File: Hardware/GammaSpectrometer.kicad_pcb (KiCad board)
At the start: 2 copper layers, 100 x 100 mm, 449 parts, among them U10 LT3093, U11 AP2112K-3.3, U12 AP2112K-1.2, U13 REF3220AMDBVREP, U14 LT3042, U15 LT3042, U16 LT8330IS6, U17 NCP163ASN330T1G (3v3), U18 5PB1102PGGK, U19 MX25L1606EM1I-12G, U2 REF3220AMDBVREP, U3 LTC6268IS6, U4 AD8139, U5 TPS7A4901, U6 ICE40HX4K-TQ144, U7 AP2112K-3.3, U7 LT8330IS6, U7 XLH736065.000000I, U8 AP2112K-1.2, U8 LT8330IS6, U9 LT3093

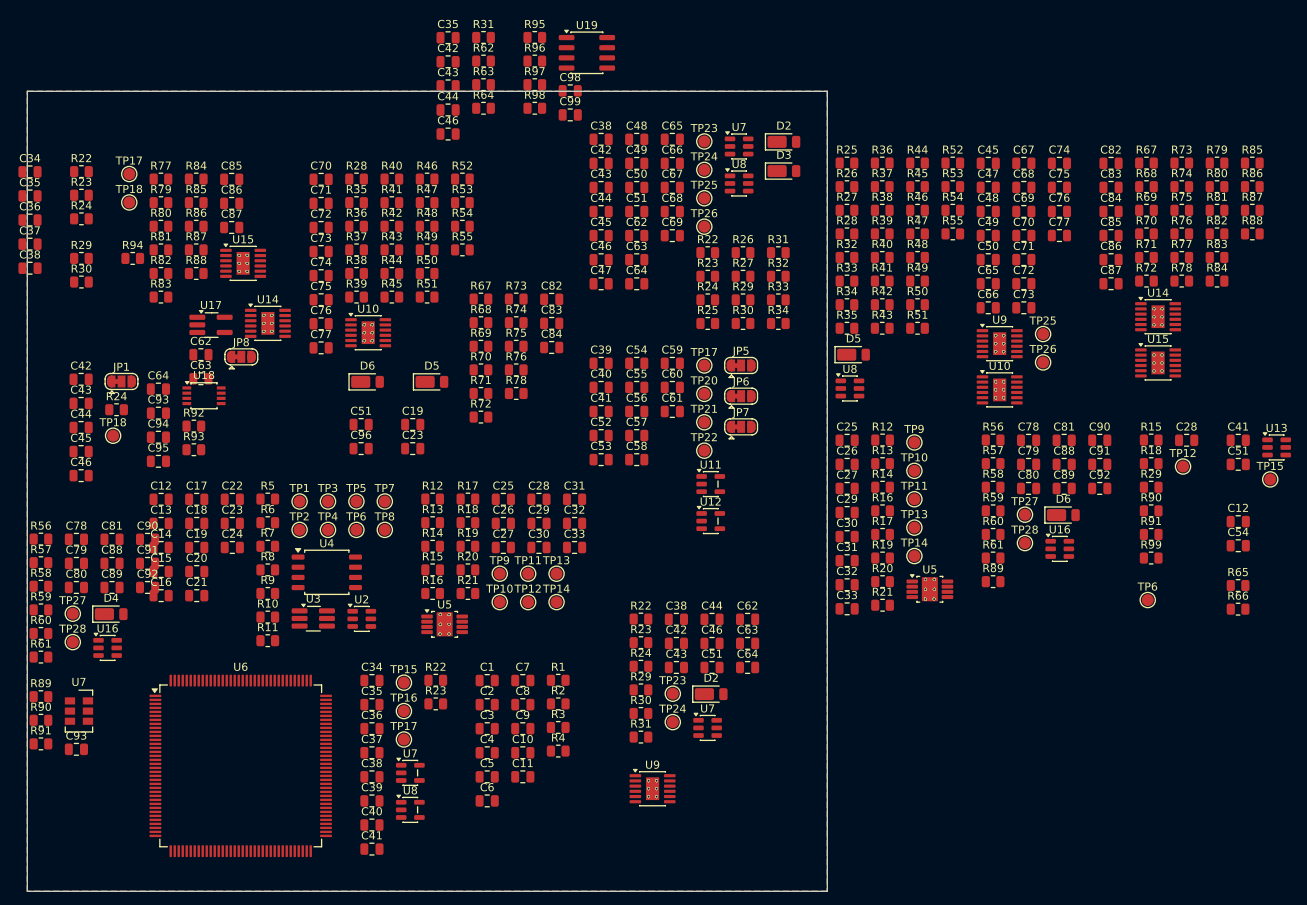
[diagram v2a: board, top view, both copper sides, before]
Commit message: fix: #134
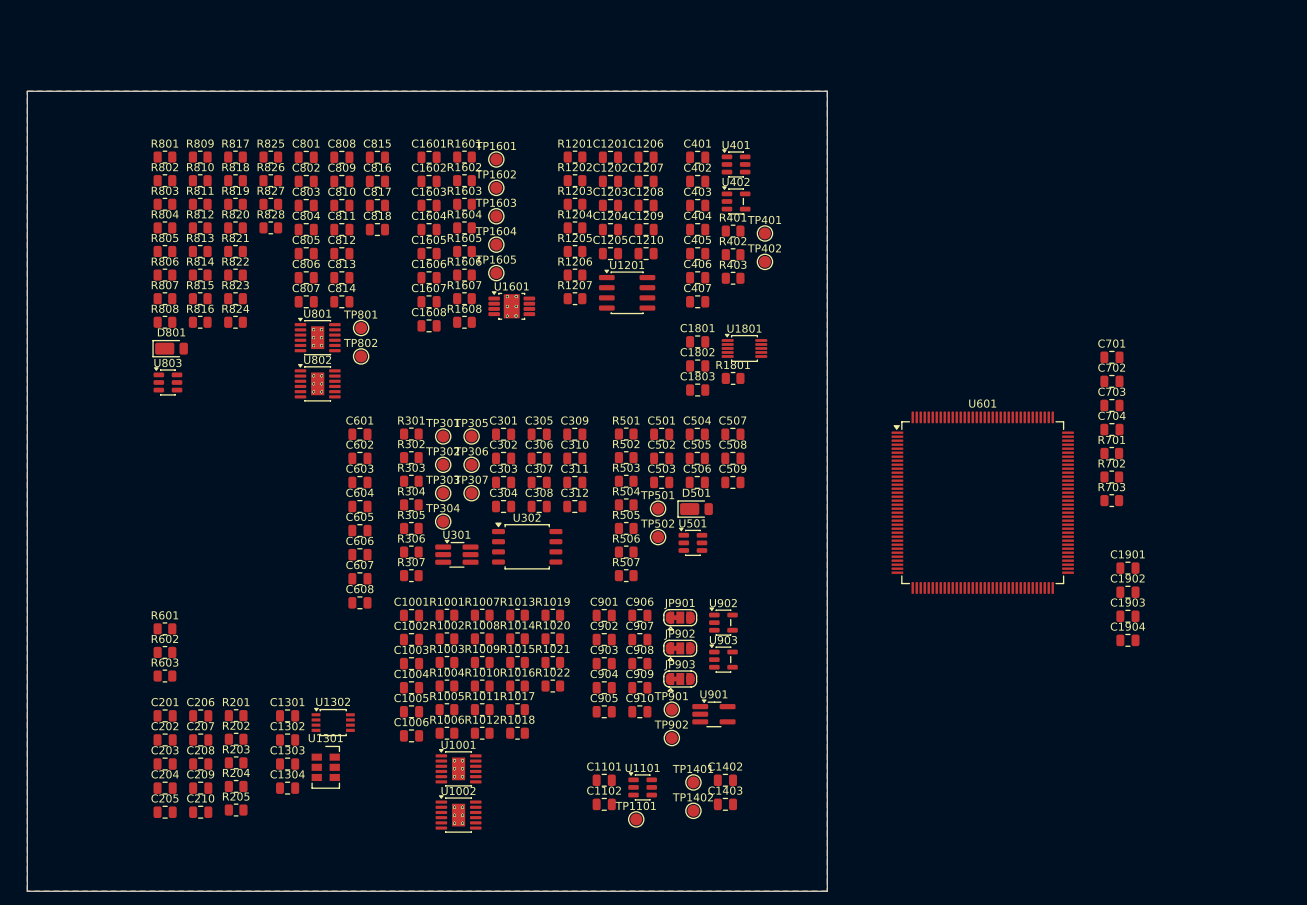
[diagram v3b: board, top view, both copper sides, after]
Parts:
- removed C1, C10, C12, C13, C14, C18, C19 (x2), C2, C28 (x2), C34, C35 (x2), C36 (x2), C37 (x2), C38, C39, C4, C41, C42, C43, C44, C46 (x3), C5, C50 (x2), C51, C52, C53, C54, C58, C59, C64 (x3), C67 (x2), C7, C80 (x2), C9, C92 (x2), C94, C96, C98: 100n, Capacitor_SMD:C_0805_2012Metric
- removed C11, C15, C16, C22, C23 (x2), C29 (x2), C30 (x2), C31 (x2), C51, C93, C95, C99: 10n, Capacitor_SMD:C_0805_2012Metric
- removed C12, C41: 470n, Capacitor_SMD:C_0805_2012Metric
- removed C17: 33p, Capacitor_SMD:C_0805_2012Metric
- removed C20, C21: 1p, Capacitor_SMD:C_0805_2012Metric
- removed C24: 22p, Capacitor_SMD:C_0805_2012Metric
- removed C25 (x2), C32 (x2): 10u/60V, Capacitor_SMD:C_0805_2012Metric
- removed C26 (x2), C33 (x2): 100n/60V, Capacitor_SMD:C_0805_2012Metric
- removed C27 (x2): TBD, Capacitor_SMD:C_0805_2012Metric
- removed C3, C38 (x2), C41, C42 (x3), C44 (x3), C46, C47 (x2), C48 (x2), C49 (x2), C51 (x2), C55, C6, C61, C62 (x2), C65 (x2), C66 (x2), C78 (x2), C79 (x2), C8, C89 (x2), C90 (x2), C91 (x2): 10u, Capacitor_SMD:C_0805_2012Metric
- removed C34, C35, C38, C39, C40 (x2), C43, C45, C54, C56, C57, C60, C62, C63 (x3), C68 (x2), C69 (x2), C81 (x2): 1u, Capacitor_SMD:C_0805_2012Metric
- removed C43 (x2), C45 (x2), C88 (x2): 10p, Capacitor_SMD:C_0805_2012Metric
- removed C70 (x2), C73 (x2), C76 (x2), C77 (x2): 4u7, Capacitor_SMD:C_0805_2012Metric
- removed C71 (x2), C75 (x2), C83 (x2), C86 (x2): 4u7 X7R, Capacitor_SMD:C_0805_2012Metric
- removed C72 (x2), C74 (x2), C82 (x2), C84 (x2), C85 (x2), C87 (x2), C93: 10u/16v, Capacitor_SMD:C_0805_2012Metric
- removed D2 (x2), D3, D4: DFLS140L-7, Diode_SMD:D_PowerDI-123
- removed D5 (x2), D6 (x2): DFLS1100-7, Diode_SMD:D_PowerDI-123
- removed JP1, JP5: DVCC_ADC_ON, Jumper:SolderJumper-3_P1.3mm_Bridged12_RoundedPad1.0x1.5mm
- removed JP6: 3V3_ON, Jumper:SolderJumper-3_P1.3mm_Bridged12_RoundedPad1.0x1.5mm
- removed JP7: 1V2_ON, Jumper:SolderJumper-3_P1.3mm_Bridged12_RoundedPad1.0x1.5mm
- removed JP8: DVCC_CLK_ON, Jumper:SolderJumper-3_P1.3mm_Bridged12_RoundedPad1.0x1.5mm
- removed R1, R13, R14 (x2), R18 (x2), R2, R22, R23, R24, R28 (x2), R29 (x2), R3, R30, R31 (x2), R34 (x2), R35 (x2), R38 (x2), R4, R40 (x2), R43 (x2), R45 (x2), R47 (x2), R48 (x2), R53 (x2), R54 (x2), R58, R65, R66, R68 (x2), R69 (x2), R70 (x2), R75 (x2), R76 (x2), R79 (x2), R80 (x2), R81 (x2), R86 (x2), R87 (x2), R89, R90 (x2), R91, R99: TBD, Resistor_SMD:R_0805_2012Metric
- removed R10, R11: 50R, Resistor_SMD:R_0805_2012Metric
- removed R12 (x2), R13, R15 (x2), R22, R23, R24 (x3), R27 (x2), R29 (x2), R30 (x2), R32 (x2), R33 (x2), R39 (x2), R41 (x2), R42 (x2), R44 (x2), R46 (x2), R49 (x2), R51 (x2), R55 (x2), R56 (x2), R57 (x2), R61 (x2), R67 (x2), R72 (x2), R74 (x2), R77 (x2), R78 (x2), R83 (x2), R85 (x2), R88 (x2), R89, R91, R92, R93, R94, R96, R97: 0R, Resistor_SMD:R_0805_2012Metric
- removed R16 (x2), R21 (x2), R23 (x2), R26 (x2), R31, R5, R60 (x2), R63, R95: 10k, Resistor_SMD:R_0805_2012Metric
- removed R17 (x2): 2M, Resistor_SMD:R_0805_2012Metric
- removed R19 (x2): 220k, Resistor_SMD:R_0805_2012Metric
- removed R20 (x2): 33k, Resistor_SMD:R_0805_2012Metric
- removed R22 (x2), R59 (x2): 200k, Resistor_SMD:R_0805_2012Metric
- removed R25 (x2): 68k1, Resistor_SMD:R_0805_2012Metric
- removed R36 (x2), R52 (x2): 19k5, Resistor_SMD:R_0805_2012Metric
- removed R37 (x2): 27k9, Resistor_SMD:R_0805_2012Metric
- removed R50 (x2), R71 (x2): 49k9, Resistor_SMD:R_0805_2012Metric
- removed R58: 47k, Resistor_SMD:R_0805_2012Metric
- removed R6, R7: 499R, Resistor_SMD:R_0805_2012Metric
- removed R62: 100R, Resistor_SMD:R_0805_2012Metric
- removed R64: 680R, Resistor_SMD:R_0805_2012Metric
- removed R73 (x2), R84 (x2): 1k24, Resistor_SMD:R_0805_2012Metric
- removed R8, R9: 1k, Resistor_SMD:R_0805_2012Metric
- removed R82 (x2): 24k9, Resistor_SMD:R_0805_2012Metric
- removed R98: 22R, Resistor_SMD:R_0805_2012Metric
- removed TP1, TP10 (x2), TP11 (x2), TP12 (x2), TP13 (x2), TP14 (x2), TP15, TP16, TP17 (x2), TP18, TP2, TP20, TP21, TP22, TP23 (x2), TP24 (x2), TP25 (x2), TP26 (x2), TP27 (x2), TP28 (x2), TP3, TP4, TP5, TP6 (x2), TP7, TP8, TP9 (x2): TestPoint, TestPoint:TestPoint_Pad_D1.5mm
- removed TP15: REF_OUT, TestPoint:TestPoint_Pad_D1.5mm
- removed TP17: GND, TestPoint:TestPoint_Pad_D1.5mm
- removed TP18: +V_IN, TestPoint:TestPoint_Pad_D1.5mm
- removed U10 (x2), U9 (x2): LT3093, Package_SO:MSOP-12-1EP_3x4.039mm_P0.65mm_EP1.651x2.845mm_ThermalVias
- removed U11, U7: AP2112K-3.3, Package_TO_SOT_SMD:SOT-23-5
- removed U12, U8: AP2112K-1.2, Package_TO_SOT_SMD:SOT-23-5
- removed U13, U2: REF3220AMDBVREP, Package_TO_SOT_SMD:SOT-23-6
- removed U14 (x2), U15 (x2): LT3042, Package_SO:MSOP-12-1EP_3x4.039mm_P0.65mm_EP1.651x2.845mm_ThermalVias
- removed U16 (x2), U7 (x2), U8 (x2): LT8330IS6, Package_TO_SOT_SMD:TSOT-23-6
- removed U17: NCP163ASN330T1G (3v3), Package_TO_SOT_SMD:TSOT-23-5_HandSoldering
- removed U18: 5PB1102PGGK, Package_SO:TSSOP-8_3x3mm_P0.65mm
- removed U19: MX25L1606EM1I-12G, Package_SO:SOP-8_3.76x4.96mm_P1.27mm
- removed U3: LTC6268IS6, Package_TO_SOT_SMD:TSOT-23-6_HandSoldering
- removed U4: AD8139, Package_SO:SOIC-8_5.3x5.3mm_P1.27mm
- removed U5 (x2): TPS7A4901, Package_SO:Texas_DGN0008B_VSSOP-8-1EP_3x3mm_P0.65mm_EP2x3mm_Mask1.88x1.98mm_ThermalVias
- removed U6: ICE40HX4K-TQ144, Package_QFP:TQFP-144_20x20mm_P0.5mm
- removed U7: XLH736065.000000I, Oscillator:Oscillator_SMD_IDT_JS6-6_5.0x3.2mm_P1.27mm
- added C1001: 10u/16v, Capacitor_SMD:C_0805_2012Metric, F.Cu at (143.0, 90.5)
- added C1002: 10u/16v, Capacitor_SMD:C_0805_2012Metric, F.Cu at (143.0, 93.5)
- added C1003: 4u7 X7R, Capacitor_SMD:C_0805_2012Metric, F.Cu at (143.0, 96.5)
- added C1004: 4u7 X7R, Capacitor_SMD:C_0805_2012Metric, F.Cu at (143.0, 99.6)
- added C1005: 10u/16v, Capacitor_SMD:C_0805_2012Metric, F.Cu at (143.0, 102.6)
- added C1006: 10u/16v, Capacitor_SMD:C_0805_2012Metric, F.Cu at (143.0, 105.6)
- added C1101: 470n, Capacitor_SMD:C_0805_2012Metric, F.Cu at (167.1, 111.1)
- added C1102: 10n, Capacitor_SMD:C_0805_2012Metric, F.Cu at (167.1, 114.1)
- added C1201: 10u, Capacitor_SMD:C_0805_2012Metric, F.Cu at (167.9, 33.3)
- added C1202: 10u, Capacitor_SMD:C_0805_2012Metric, F.Cu at (167.9, 36.3)
- added C1203: 10u, Capacitor_SMD:C_0805_2012Metric, F.Cu at (167.9, 39.3)
- added C1204: 100n, Capacitor_SMD:C_0805_2012Metric, F.Cu at (167.9, 42.3)
- added C1205: 100n, Capacitor_SMD:C_0805_2012Metric, F.Cu at (167.9, 45.3)
- added C1206: 100n, Capacitor_SMD:C_0805_2012Metric, F.Cu at (172.3, 33.3)
- added C1207: 100n, Capacitor_SMD:C_0805_2012Metric, F.Cu at (172.3, 36.3)
- added C1208: 100n, Capacitor_SMD:C_0805_2012Metric, F.Cu at (172.3, 39.3)
- added C1209: 100n, Capacitor_SMD:C_0805_2012Metric, F.Cu at (172.3, 42.3)
- added C1210: 10n, Capacitor_SMD:C_0805_2012Metric, F.Cu at (172.3, 45.3)
- added C1301: 100n, Capacitor_SMD:C_0805_2012Metric, F.Cu at (127.5, 103.1)
- added C1302: 10n, Capacitor_SMD:C_0805_2012Metric, F.Cu at (127.5, 106.1)
- added C1303: 100n, Capacitor_SMD:C_0805_2012Metric, F.Cu at (127.5, 109.1)
- added C1304: 10n, Capacitor_SMD:C_0805_2012Metric, F.Cu at (127.5, 112.1)
- added C1402: 100n, Capacitor_SMD:C_0805_2012Metric, F.Cu at (182.3, 111.1)
- added C1403: 100n, Capacitor_SMD:C_0805_2012Metric, F.Cu at (182.3, 114.1)
- added C1601: 10u/60V, Capacitor_SMD:C_0805_2012Metric, F.Cu at (145.2, 33.3)
- added C1602: 100n/60V, Capacitor_SMD:C_0805_2012Metric, F.Cu at (145.2, 36.3)
- added C1603: TBD, Capacitor_SMD:C_0805_2012Metric, F.Cu at (145.2, 39.3)
- added C1604: 10n, Capacitor_SMD:C_0805_2012Metric, F.Cu at (145.2, 42.3)
- added C1605: 10n, Capacitor_SMD:C_0805_2012Metric, F.Cu at (145.2, 45.3)
- added C1606: 10n, Capacitor_SMD:C_0805_2012Metric, F.Cu at (145.2, 48.3)
- added C1607: 10u/60V, Capacitor_SMD:C_0805_2012Metric, F.Cu at (145.2, 51.3)
- added C1608: 100n/60V, Capacitor_SMD:C_0805_2012Metric, F.Cu at (145.2, 54.3)
- added C1801: 10u, Capacitor_SMD:C_0805_2012Metric, F.Cu at (178.8, 56.3)
- added C1802: 100n, Capacitor_SMD:C_0805_2012Metric, F.Cu at (178.8, 59.3)
- added C1803: 100n, Capacitor_SMD:C_0805_2012Metric, F.Cu at (178.8, 62.3)
- added C1901: 10u, Capacitor_SMD:C_0805_2012Metric, F.Cu at (232.6, 84.6)
- added C1902: 100n, Capacitor_SMD:C_0805_2012Metric, F.Cu at (232.6, 87.6)
- added C1903: 10u, Capacitor_SMD:C_0805_2012Metric, F.Cu at (232.6, 90.6)
- added C1904: 100n, Capacitor_SMD:C_0805_2012Metric, F.Cu at (232.6, 93.6)
- added C201: 100n, Capacitor_SMD:C_0805_2012Metric, F.Cu at (112.2, 103.1)
- added C202: 10u, Capacitor_SMD:C_0805_2012Metric, F.Cu at (112.2, 106.1)
- added C203: 100n, Capacitor_SMD:C_0805_2012Metric, F.Cu at (112.2, 109.1)
- added C204: 100n, Capacitor_SMD:C_0805_2012Metric, F.Cu at (112.2, 112.1)
- added C205: 100n, Capacitor_SMD:C_0805_2012Metric, F.Cu at (112.2, 115.1)
- added C206: 10u, Capacitor_SMD:C_0805_2012Metric, F.Cu at (116.7, 103.1)
- added C207: 10u, Capacitor_SMD:C_0805_2012Metric, F.Cu at (116.7, 106.1)
- added C208: 100n, Capacitor_SMD:C_0805_2012Metric, F.Cu at (116.7, 109.1)
- added C209: 100n, Capacitor_SMD:C_0805_2012Metric, F.Cu at (116.7, 112.1)
- added C210: 10n, Capacitor_SMD:C_0805_2012Metric, F.Cu at (116.7, 115.1)
- added C301: 100n, Capacitor_SMD:C_0805_2012Metric, F.Cu at (154.5, 67.9)
- added C302: 100n, Capacitor_SMD:C_0805_2012Metric, F.Cu at (154.5, 70.9)
- added C303: 10n, Capacitor_SMD:C_0805_2012Metric, F.Cu at (154.5, 73.9)
- added C304: 10n, Capacitor_SMD:C_0805_2012Metric, F.Cu at (154.5, 76.9)
- added C305: 33p, Capacitor_SMD:C_0805_2012Metric, F.Cu at (159.0, 67.9)
- added C306: 100n, Capacitor_SMD:C_0805_2012Metric, F.Cu at (159.0, 70.9)
- added C307: 100n, Capacitor_SMD:C_0805_2012Metric, F.Cu at (159.0, 73.9)
- added C308: 1p, Capacitor_SMD:C_0805_2012Metric, F.Cu at (159.0, 76.9)
- added C309: 1p, Capacitor_SMD:C_0805_2012Metric, F.Cu at (163.4, 67.9)
- added C310: 10n, Capacitor_SMD:C_0805_2012Metric, F.Cu at (163.4, 70.9)
- added C311: 10n, Capacitor_SMD:C_0805_2012Metric, F.Cu at (163.4, 73.9)
- added C312: 22p, Capacitor_SMD:C_0805_2012Metric, F.Cu at (163.4, 76.9)
- added C401: 10u, Capacitor_SMD:C_0805_2012Metric, F.Cu at (178.8, 33.3)
- added C402: 10u, Capacitor_SMD:C_0805_2012Metric, F.Cu at (178.8, 36.3)
- added C403: TBD, Capacitor_SMD:C_0805_2012Metric, F.Cu at (178.8, 39.3)
- added C404: 100n, Capacitor_SMD:C_0805_2012Metric, F.Cu at (178.8, 42.3)
- added C405: 100n, Capacitor_SMD:C_0805_2012Metric, F.Cu at (178.8, 45.3)
- added C406: 10n, Capacitor_SMD:C_0805_2012Metric, F.Cu at (178.8, 48.3)
- added C407: 10n, Capacitor_SMD:C_0805_2012Metric, F.Cu at (178.8, 51.3)
- added C501: 10u, Capacitor_SMD:C_0805_2012Metric, F.Cu at (174.3, 67.9)
- added C502: 10u, Capacitor_SMD:C_0805_2012Metric, F.Cu at (174.3, 70.9)
- added C503: 100n, Capacitor_SMD:C_0805_2012Metric, F.Cu at (174.3, 73.9)
- added C504: 1u, Capacitor_SMD:C_0805_2012Metric, F.Cu at (178.7, 67.9)
- added C505: 10p, Capacitor_SMD:C_0805_2012Metric, F.Cu at (178.7, 70.9)
- added C506: 10u, Capacitor_SMD:C_0805_2012Metric, F.Cu at (178.7, 73.9)
- added C507: 10u, Capacitor_SMD:C_0805_2012Metric, F.Cu at (183.2, 67.9)
- added C508: 10u, Capacitor_SMD:C_0805_2012Metric, F.Cu at (183.2, 70.9)
- added C509: 100n, Capacitor_SMD:C_0805_2012Metric, F.Cu at (183.2, 73.9)
- added C601: 100n, Capacitor_SMD:C_0805_2012Metric, F.Cu at (136.6, 67.9)
- added C602: 100n, Capacitor_SMD:C_0805_2012Metric, F.Cu at (136.6, 70.9)
- added C603: 100n, Capacitor_SMD:C_0805_2012Metric, F.Cu at (136.6, 73.9)
- added C604: 100n, Capacitor_SMD:C_0805_2012Metric, F.Cu at (136.6, 76.9)
- added C605: 10u, Capacitor_SMD:C_0805_2012Metric, F.Cu at (136.6, 79.9)
- added C606: 10u, Capacitor_SMD:C_0805_2012Metric, F.Cu at (136.6, 82.9)
- added C607: 10u, Capacitor_SMD:C_0805_2012Metric, F.Cu at (136.6, 85.9)
- added C608: 10u, Capacitor_SMD:C_0805_2012Metric, F.Cu at (136.6, 88.9)
- added C701: 10u, Capacitor_SMD:C_0805_2012Metric, F.Cu at (230.6, 58.3)
- added C702: 100n, Capacitor_SMD:C_0805_2012Metric, F.Cu at (230.6, 61.3)
- added C703: 10u, Capacitor_SMD:C_0805_2012Metric, F.Cu at (230.6, 64.3)
- added C704: 100n, Capacitor_SMD:C_0805_2012Metric, F.Cu at (230.6, 67.3)
- added C801: 10u, Capacitor_SMD:C_0805_2012Metric, F.Cu at (129.9, 33.3)
- added C802: 10u/16v, Capacitor_SMD:C_0805_2012Metric, F.Cu at (129.9, 36.3)
- added C803: 10u/16v, Capacitor_SMD:C_0805_2012Metric, F.Cu at (129.9, 39.3)
- added C804: 10u, Capacitor_SMD:C_0805_2012Metric, F.Cu at (129.9, 42.3)
- added C805: 100n, Capacitor_SMD:C_0805_2012Metric, F.Cu at (129.9, 45.3)
- added C806: 4u7 X7R, Capacitor_SMD:C_0805_2012Metric, F.Cu at (129.9, 48.3)
- added C807: 4u7 X7R, Capacitor_SMD:C_0805_2012Metric, F.Cu at (129.9, 51.3)
- added C808: 1u, Capacitor_SMD:C_0805_2012Metric, F.Cu at (134.3, 33.3)
- added C809: 1u, Capacitor_SMD:C_0805_2012Metric, F.Cu at (134.3, 36.3)
- added C810: 4u7, Capacitor_SMD:C_0805_2012Metric, F.Cu at (134.3, 39.3)
- added C811: 4u7, Capacitor_SMD:C_0805_2012Metric, F.Cu at (134.3, 42.3)
- added C812: 4u7, Capacitor_SMD:C_0805_2012Metric, F.Cu at (134.3, 45.3)
- added C813: 4u7, Capacitor_SMD:C_0805_2012Metric, F.Cu at (134.3, 48.3)
- added C814: 10p, Capacitor_SMD:C_0805_2012Metric, F.Cu at (134.3, 51.3)
- added C815: 10u, Capacitor_SMD:C_0805_2012Metric, F.Cu at (138.8, 33.3)
- added C816: 10u, Capacitor_SMD:C_0805_2012Metric, F.Cu at (138.8, 36.3)
- added C817: 100n, Capacitor_SMD:C_0805_2012Metric, F.Cu at (138.8, 39.3)
- added C818: 10u, Capacitor_SMD:C_0805_2012Metric, F.Cu at (138.8, 42.3)
- added C901: 1u, Capacitor_SMD:C_0805_2012Metric, F.Cu at (167.1, 90.5)
- added C902: 1u, Capacitor_SMD:C_0805_2012Metric, F.Cu at (167.1, 93.5)
- added C903: 1u, Capacitor_SMD:C_0805_2012Metric, F.Cu at (167.1, 96.5)
- added C904: 100n, Capacitor_SMD:C_0805_2012Metric, F.Cu at (167.1, 99.6)
- added C905: 100n, Capacitor_SMD:C_0805_2012Metric, F.Cu at (167.1, 102.6)
- added C906: 1u, Capacitor_SMD:C_0805_2012Metric, F.Cu at (171.6, 90.5)
- added C907: 1u, Capacitor_SMD:C_0805_2012Metric, F.Cu at (171.6, 93.5)
- added C908: 1u, Capacitor_SMD:C_0805_2012Metric, F.Cu at (171.6, 96.5)
- added C909: 100n, Capacitor_SMD:C_0805_2012Metric, F.Cu at (171.6, 99.6)
- added C910: 100n, Capacitor_SMD:C_0805_2012Metric, F.Cu at (171.6, 102.6)
- added D501: DFLS1100-7, Diode_SMD:D_PowerDI-123, F.Cu at (178.6, 77.2)
- added D801: DFLS1100-7, Diode_SMD:D_PowerDI-123, F.Cu at (113.0, 57.2)
- added JP901: DVCC_CLK_ON, Jumper:SolderJumper-3_P1.3mm_Bridged12_RoundedPad1.0x1.5mm, F.Cu at (176.6, 90.8)
- added JP902: 3V3_ON, Jumper:SolderJumper-3_P1.3mm_Bridged12_RoundedPad1.0x1.5mm, F.Cu at (176.6, 94.6)
- added JP903: 1V2_ON, Jumper:SolderJumper-3_P1.3mm_Bridged12_RoundedPad1.0x1.5mm, F.Cu at (176.6, 98.5)
- added R1001: 0R, Resistor_SMD:R_0805_2012Metric, F.Cu at (147.5, 90.5)
- added R1002: TBD, Resistor_SMD:R_0805_2012Metric, F.Cu at (147.5, 93.4)
- added R1003: 0R, Resistor_SMD:R_0805_2012Metric, F.Cu at (147.5, 96.4)
- added R1004: TBD, Resistor_SMD:R_0805_2012Metric, F.Cu at (147.5, 99.3)
- added R1005: TBD, Resistor_SMD:R_0805_2012Metric, F.Cu at (147.5, 102.3)
- added R1006: TBD, Resistor_SMD:R_0805_2012Metric, F.Cu at (147.5, 105.2)
- added R1007: TBD, Resistor_SMD:R_0805_2012Metric, F.Cu at (151.9, 90.5)
- added R1008: TBD, Resistor_SMD:R_0805_2012Metric, F.Cu at (151.9, 93.4)
- added R1009: 49k9, Resistor_SMD:R_0805_2012Metric, F.Cu at (151.9, 96.4)
- added R1010: 0R, Resistor_SMD:R_0805_2012Metric, F.Cu at (151.9, 99.3)
- added R1011: 24k9, Resistor_SMD:R_0805_2012Metric, F.Cu at (151.9, 102.3)
- added R1012: 0R, Resistor_SMD:R_0805_2012Metric, F.Cu at (151.9, 105.2)
- added R1013: 1k24, Resistor_SMD:R_0805_2012Metric, F.Cu at (156.3, 90.5)
- added R1014: 0R, Resistor_SMD:R_0805_2012Metric, F.Cu at (156.3, 93.4)
- added R1015: 1k24, Resistor_SMD:R_0805_2012Metric, F.Cu at (156.3, 96.4)
- added R1016: 0R, Resistor_SMD:R_0805_2012Metric, F.Cu at (156.3, 99.3)
- added R1017: TBD, Resistor_SMD:R_0805_2012Metric, F.Cu at (156.3, 102.3)
- added R1018: TBD, Resistor_SMD:R_0805_2012Metric, F.Cu at (156.3, 105.2)
- added R1019: TBD, Resistor_SMD:R_0805_2012Metric, F.Cu at (160.7, 90.5)
- added R1020: TBD, Resistor_SMD:R_0805_2012Metric, F.Cu at (160.7, 93.4)
- added R1021: 0R, Resistor_SMD:R_0805_2012Metric, F.Cu at (160.7, 96.4)
- added R1022: 0R, Resistor_SMD:R_0805_2012Metric, F.Cu at (160.7, 99.3)
- added R1201: 10k, Resistor_SMD:R_0805_2012Metric, F.Cu at (163.5, 33.2)
- added R1202: 100R, Resistor_SMD:R_0805_2012Metric, F.Cu at (163.5, 36.2)
- added R1203: 10k, Resistor_SMD:R_0805_2012Metric, F.Cu at (163.5, 39.1)
- added R1204: 22R, Resistor_SMD:R_0805_2012Metric, F.Cu at (163.5, 42.1)
- added R1205: 0R, Resistor_SMD:R_0805_2012Metric, F.Cu at (163.5, 45.0)
- added R1206: 0R, Resistor_SMD:R_0805_2012Metric, F.Cu at (163.5, 48.0)
- added R1207: 10k, Resistor_SMD:R_0805_2012Metric, F.Cu at (163.5, 50.9)
- added R1601: 0R, Resistor_SMD:R_0805_2012Metric, F.Cu at (149.6, 33.2)
- added R1602: 0R, Resistor_SMD:R_0805_2012Metric, F.Cu at (149.6, 36.2)
- added R1603: TBD, Resistor_SMD:R_0805_2012Metric, F.Cu at (149.6, 39.1)
- added R1604: 10k, Resistor_SMD:R_0805_2012Metric, F.Cu at (149.6, 42.1)
- added R1605: 2M, Resistor_SMD:R_0805_2012Metric, F.Cu at (149.6, 45.0)
- added R1606: 220k, Resistor_SMD:R_0805_2012Metric, F.Cu at (149.6, 48.0)
- added R1607: 33k, Resistor_SMD:R_0805_2012Metric, F.Cu at (149.6, 50.9)
- added R1608: 10k, Resistor_SMD:R_0805_2012Metric, F.Cu at (149.6, 53.9)
- added R1801: 10k, Resistor_SMD:R_0805_2012Metric, F.Cu at (183.2, 60.9)
- added R201: TBD, Resistor_SMD:R_0805_2012Metric, F.Cu at (121.1, 103.0)
- added R202: TBD, Resistor_SMD:R_0805_2012Metric, F.Cu at (121.1, 106.0)
- added R203: TBD, Resistor_SMD:R_0805_2012Metric, F.Cu at (121.1, 108.9)
- added R204: TBD, Resistor_SMD:R_0805_2012Metric, F.Cu at (121.1, 111.9)
- added R205: TBD, Resistor_SMD:R_0805_2012Metric, F.Cu at (121.1, 114.8)
- added R301: 10k, Resistor_SMD:R_0805_2012Metric, F.Cu at (143.0, 67.8)
- added R302: 499R, Resistor_SMD:R_0805_2012Metric, F.Cu at (143.0, 70.8)
- added R303: 499R, Resistor_SMD:R_0805_2012Metric, F.Cu at (143.0, 73.7)
- added R304: 1k, Resistor_SMD:R_0805_2012Metric, F.Cu at (143.0, 76.7)
- added R305: 1k, Resistor_SMD:R_0805_2012Metric, F.Cu at (143.0, 79.6)
- added R306: 50R, Resistor_SMD:R_0805_2012Metric, F.Cu at (143.0, 82.6)
- added R307: 50R, Resistor_SMD:R_0805_2012Metric, F.Cu at (143.0, 85.5)
- added R401: TBD, Resistor_SMD:R_0805_2012Metric, F.Cu at (183.2, 42.5)
- added R402: TBD, Resistor_SMD:R_0805_2012Metric, F.Cu at (183.2, 45.4)
- added R403: TBD, Resistor_SMD:R_0805_2012Metric, F.Cu at (183.2, 48.4)
- added R501: 0R, Resistor_SMD:R_0805_2012Metric, F.Cu at (169.9, 67.8)
- added R502: 0R, Resistor_SMD:R_0805_2012Metric, F.Cu at (169.9, 70.8)
- added R503: TBD, Resistor_SMD:R_0805_2012Metric, F.Cu at (169.9, 73.7)
- added R504: 47k, Resistor_SMD:R_0805_2012Metric, F.Cu at (169.9, 76.7)
- added R505: 200k, Resistor_SMD:R_0805_2012Metric, F.Cu at (169.9, 79.6)
- added R506: 10k, Resistor_SMD:R_0805_2012Metric, F.Cu at (169.9, 82.6)
- added R507: 0R, Resistor_SMD:R_0805_2012Metric, F.Cu at (169.9, 85.5)
- added R601: 2k2, Resistor_SMD:R_0805_2012Metric, F.Cu at (112.2, 92.2)
- added R602: 2k2, Resistor_SMD:R_0805_2012Metric, F.Cu at (112.2, 95.1)
- added R603: 680R, Resistor_SMD:R_0805_2012Metric, F.Cu at (112.2, 98.1)
- added R701: 2k2, Resistor_SMD:R_0805_2012Metric, F.Cu at (230.6, 70.3)
- added R702: 2k2, Resistor_SMD:R_0805_2012Metric, F.Cu at (230.6, 73.2)
- added R703: 680R, Resistor_SMD:R_0805_2012Metric, F.Cu at (230.6, 76.2)
- added R801: 0R, Resistor_SMD:R_0805_2012Metric, F.Cu at (112.2, 33.2)
- added R802: TBD, Resistor_SMD:R_0805_2012Metric, F.Cu at (112.2, 36.2)
- added R803: 0R, Resistor_SMD:R_0805_2012Metric, F.Cu at (112.2, 39.1)
- added R804: TBD, Resistor_SMD:R_0805_2012Metric, F.Cu at (112.2, 42.1)
- added R805: 0R, Resistor_SMD:R_0805_2012Metric, F.Cu at (112.2, 45.0)
- added R806: TBD, Resistor_SMD:R_0805_2012Metric, F.Cu at (112.2, 48.0)
- added R807: TBD, Resistor_SMD:R_0805_2012Metric, F.Cu at (112.2, 50.9)
- added R808: TBD, Resistor_SMD:R_0805_2012Metric, F.Cu at (112.2, 53.9)
- added R809: TBD, Resistor_SMD:R_0805_2012Metric, F.Cu at (116.6, 33.2)
- added R810: 0R, Resistor_SMD:R_0805_2012Metric, F.Cu at (116.6, 36.2)
- added R811: TBD, Resistor_SMD:R_0805_2012Metric, F.Cu at (116.6, 39.1)
- added R812: 0R, Resistor_SMD:R_0805_2012Metric, F.Cu at (116.6, 42.1)
- added R813: 27k9, Resistor_SMD:R_0805_2012Metric, F.Cu at (116.6, 45.0)
- added R814: 0R, Resistor_SMD:R_0805_2012Metric, F.Cu at (116.6, 48.0)
- added R815: 49k9, Resistor_SMD:R_0805_2012Metric, F.Cu at (116.6, 50.9)
- added R816: 0R, Resistor_SMD:R_0805_2012Metric, F.Cu at (116.6, 53.9)
- added R817: 19k5, Resistor_SMD:R_0805_2012Metric, F.Cu at (121.0, 33.2)
- added R818: 0R, Resistor_SMD:R_0805_2012Metric, F.Cu at (121.0, 36.2)
- added R819: 19k5, Resistor_SMD:R_0805_2012Metric, F.Cu at (121.0, 39.1)
- added R820: TBD, Resistor_SMD:R_0805_2012Metric, F.Cu at (121.0, 42.1)
- added R821: TBD, Resistor_SMD:R_0805_2012Metric, F.Cu at (121.0, 45.0)
- added R822: TBD, Resistor_SMD:R_0805_2012Metric, F.Cu at (121.0, 48.0)
- added R823: TBD, Resistor_SMD:R_0805_2012Metric, F.Cu at (121.0, 50.9)
- added R824: 0R, Resistor_SMD:R_0805_2012Metric, F.Cu at (121.0, 53.9)
- added R825: 0R, Resistor_SMD:R_0805_2012Metric, F.Cu at (125.4, 33.2)
- added R826: 68k1, Resistor_SMD:R_0805_2012Metric, F.Cu at (125.4, 36.2)
- added R827: 10k, Resistor_SMD:R_0805_2012Metric, F.Cu at (125.4, 39.1)
- added R828: 0R, Resistor_SMD:R_0805_2012Metric, F.Cu at (125.4, 42.1)
- added TP1101: REF_OUT, TestPoint:TestPoint_Pad_D1.5mm, F.Cu at (171.1, 116.0)
- added TP1401: +V_IN, TestPoint:TestPoint_Pad_D1.5mm, F.Cu at (178.3, 111.4)
- added TP1402: GND, TestPoint:TestPoint_Pad_D1.5mm, F.Cu at (178.3, 114.9)
- added TP1601: TestPoint, TestPoint:TestPoint_Pad_D1.5mm, F.Cu at (153.6, 33.5)
- added TP1602: TestPoint, TestPoint:TestPoint_Pad_D1.5mm, F.Cu at (153.6, 37.1)
- added TP1603: TestPoint, TestPoint:TestPoint_Pad_D1.5mm, F.Cu at (153.6, 40.6)
- added TP1604: TestPoint, TestPoint:TestPoint_Pad_D1.5mm, F.Cu at (153.6, 44.2)
- added TP1605: TestPoint, TestPoint:TestPoint_Pad_D1.5mm, F.Cu at (153.6, 47.7)
- added TP301: TestPoint, TestPoint:TestPoint_Pad_D1.5mm, F.Cu at (147.0, 68.1)
- added TP302: TestPoint, TestPoint:TestPoint_Pad_D1.5mm, F.Cu at (147.0, 71.7)
- added TP303: TestPoint, TestPoint:TestPoint_Pad_D1.5mm, F.Cu at (147.0, 75.2)
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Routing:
- added copper zone on B.Cu, net (none)
- added copper zone on F.Cu, net (none)
- removed copper zone on B.Cu, net GNDD
- removed copper zone on F.Cu, net GNDD

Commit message: fix: #170, fix #144
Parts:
- removed C1001, C1005, C802: 10u/16v, Capacitor_SMD:C_0805_2012Metric
- removed C1003, C806: 4u7 X7R, Capacitor_SMD:C_0805_2012Metric
- removed C301, C302, C306, C307, C601, C602, C603, C604: 100n, Capacitor_SMD:C_0805_2012Metric
- removed C303, C304, C310, C311: 10n, Capacitor_SMD:C_0805_2012Metric
- removed C305: 33p, Capacitor_SMD:C_0805_2012Metric
- removed C308, C309: 1p, Capacitor_SMD:C_0805_2012Metric
- removed C312: 22p, Capacitor_SMD:C_0805_2012Metric
- removed C605, C606, C607, C608: 10u, Capacitor_SMD:C_0805_2012Metric
- removed C810, C812: 4u7, Capacitor_SMD:C_0805_2012Metric
- removed R1001, R1010, R1014, R1021, R803, R812, R816, R824: 0R, Resistor_SMD:R_0805_2012Metric
- removed R1002, R1005, R1006, R1017, R1018, R802, R806, R807, R820, R821: TBD, Resistor_SMD:R_0805_2012Metric
- removed R1009: 49k9, Resistor_SMD:R_0805_2012Metric
- removed R1013: 1k24, Resistor_SMD:R_0805_2012Metric
- removed R301: 10k, Resistor_SMD:R_0805_2012Metric
- removed R302, R303: 499R, Resistor_SMD:R_0805_2012Metric
- removed R304, R305: 1k, Resistor_SMD:R_0805_2012Metric
- removed R306, R307: 50R, Resistor_SMD:R_0805_2012Metric
- removed R601, R602: 2k2, Resistor_SMD:R_0805_2012Metric
- removed R603: 680R, Resistor_SMD:R_0805_2012Metric
- removed R813: 27k9, Resistor_SMD:R_0805_2012Metric
- removed R817: 19k5, Resistor_SMD:R_0805_2012Metric
- removed TP301, TP302, TP303, TP304, TP305, TP306, TP307: TestPoint, TestPoint:TestPoint_Pad_D1.5mm
- removed U1001: LT3042, Package_SO:MSOP-12-1EP_3x4.039mm_P0.65mm_EP1.651x2.845mm_ThermalVias
- removed U301: LTC6268IS6, Package_TO_SOT_SMD:TSOT-23-6_HandSoldering
- removed U302: AD8139, Package_SO:SOIC-8_5.3x5.3mm_P1.27mm
- removed U801: LT3093, Package_SO:MSOP-12-1EP_3x4.039mm_P0.65mm_EP1.651x2.845mm_ThermalVias
- added C2001: 100n, Capacitor_SMD:C_0805_2012Metric, F.Cu at (105.0, 36.5)
- added C2002: 100n, Capacitor_SMD:C_0805_2012Metric, F.Cu at (112.9, 33.3)
- added C2003: 33p, Capacitor_SMD:C_0805_2012Metric, F.Cu at (108.6, 31.1)
- added C2004: 10n, Capacitor_SMD:C_0805_2012Metric, F.Cu at (105.0, 34.3)
- added C2005: 10n, Capacitor_SMD:C_0805_2012Metric, F.Cu at (112.9, 35.5)
- added C2006: 100n, Capacitor_SMD:C_0805_2012Metric, F.Cu at (100.6, 43.0)
- added C2007: 100n, Capacitor_SMD:C_0805_2012Metric, F.Cu at (113.6, 41.9)
- added C2008: 1p, Capacitor_SMD:C_0805_2012Metric, F.Cu at (110.0, 48.5)
- added C2009: 1p, Capacitor_SMD:C_0805_2012Metric, F.Cu at (104.0, 48.5)
- added C2010: 10n, Capacitor_SMD:C_0805_2012Metric, F.Cu at (100.6, 45.1)
- added C2011: 10n, Capacitor_SMD:C_0805_2012Metric, F.Cu at (113.6, 44.1)
- added C2012: 22p, Capacitor_SMD:C_0805_2012Metric, F.Cu at (107.0, 53.3)
- added C2013: TBD, Capacitor_SMD:C_0805_2012Metric, F.Cu at (107.0, 58.1)
- added C2014: 100n, Capacitor_SMD:C_0805_2012Metric, F.Cu at (100.6, 38.8)
- added C2015: 10n, Capacitor_SMD:C_0805_2012Metric, F.Cu at (100.6, 40.9)
- added C2016: TBD, Capacitor_SMD:C_0805_2012Metric, F.Cu at (110.6, 58.5)
- added C2017: TBD, Capacitor_SMD:C_0805_2012Metric, F.Cu at (103.2, 58.7)
- added C2101: 33p, Capacitor_SMD:C_0805_2012Metric, F.Cu at (131.0, 33.4)
- added C2102: 100n, Capacitor_SMD:C_0805_2012Metric, F.Cu at (127.4, 38.8)
- added C2103: 100n, Capacitor_SMD:C_0805_2012Metric, F.Cu at (135.3, 35.6)
- added C2104: 100n, Capacitor_SMD:C_0805_2012Metric, F.Cu at (123.0, 41.1)
- added C2105: 10n, Capacitor_SMD:C_0805_2012Metric, F.Cu at (127.4, 36.6)
- added C2106: 10n, Capacitor_SMD:C_0805_2012Metric, F.Cu at (135.3, 37.8)
- added C2107: 10n, Capacitor_SMD:C_0805_2012Metric, F.Cu at (123.0, 43.2)
- added C2108: 1p, Capacitor_SMD:C_0805_2012Metric, F.Cu at (132.4, 50.8)
- added C2109: 1p, Capacitor_SMD:C_0805_2012Metric, F.Cu at (126.4, 50.8)
- added C2110: 100n, Capacitor_SMD:C_0805_2012Metric, F.Cu at (123.0, 45.3)
- added C2111: 100n, Capacitor_SMD:C_0805_2012Metric, F.Cu at (136.0, 44.2)
- added C2112: 10n, Capacitor_SMD:C_0805_2012Metric, F.Cu at (123.0, 47.4)
- added C2113: 10n, Capacitor_SMD:C_0805_2012Metric, F.Cu at (136.0, 46.4)
- added C2114: 22p, Capacitor_SMD:C_0805_2012Metric, F.Cu at (129.4, 55.6)
- added C2115: TBD, Capacitor_SMD:C_0805_2012Metric, F.Cu at (133.0, 60.8)
- added C2116: TBD, Capacitor_SMD:C_0805_2012Metric, F.Cu at (129.4, 60.4)
- added C2117: TBD, Capacitor_SMD:C_0805_2012Metric, F.Cu at (125.5, 61.0)
- added C911: 1u, Capacitor_SMD:C_0805_2012Metric, F.Cu at (264.9, 28.0)
- added C912: 100n, Capacitor_SMD:C_0805_2012Metric, F.Cu at (265.2, 49.0)
- added C913: 1u, Capacitor_SMD:C_0805_2012Metric, F.Cu at (269.7, 34.0)
- added C914: 100n, Capacitor_SMD:C_0805_2012Metric, F.Cu at (269.7, 37.0)
- added C915: 100n, Capacitor_SMD:C_0805_2012Metric, F.Cu at (269.7, 40.0)
- added C916: 100n, Capacitor_SMD:C_0805_2012Metric, F.Cu at (269.7, 43.0)
- added C917: 100n, Capacitor_SMD:C_0805_2012Metric, F.Cu at (269.7, 46.0)
- added C918: 100n, Capacitor_SMD:C_0805_2012Metric, F.Cu at (269.7, 49.0)
- added C919: 100n, Capacitor_SMD:C_0805_2012Metric, F.Cu at (274.1, 34.0)
- added C920: 100n, Capacitor_SMD:C_0805_2012Metric, F.Cu at (274.1, 37.0)
- added C921: 100n, Capacitor_SMD:C_0805_2012Metric, F.Cu at (274.1, 40.0)
- added C922: 100n, Capacitor_SMD:C_0805_2012Metric, F.Cu at (274.1, 43.0)
- added J1801: USB_B_Micro, GammaSpectrometer:USB_Micro-B_Molex-105017-0001_Extra_Mechanical_Pads, F.Cu at (256.8, 141.5)
- added JP904: 1V2_ON, Jumper:SolderJumper-3_P1.3mm_Bridged12_RoundedPad1.0x1.5mm, F.Cu at (255.8, 45.8)
- added JP906: 1V2_ON, Jumper:SolderJumper-3_P1.3mm_Bridged12_RoundedPad1.0x1.5mm, F.Cu at (255.8, 49.6)
- added R2001: 10k, Resistor_SMD:R_0805_2012Metric, F.Cu at (108.6, 33.1)
- added R2101: 10k, Resistor_SMD:R_0805_2012Metric, F.Cu at (131.0, 35.4)
- added R901: TBD, Resistor_SMD:R_0805_2012Metric, F.Cu at (250.7, 34.0)
- added R902: TBD, Resistor_SMD:R_0805_2012Metric, F.Cu at (250.7, 36.9)
- added R903: TBD, Resistor_SMD:R_0805_2012Metric, F.Cu at (250.7, 39.9)
- added R904: TBD, Resistor_SMD:R_0805_2012Metric, F.Cu at (250.7, 42.8)
- added R905: TBD, Resistor_SMD:R_0805_2012Metric, F.Cu at (250.7, 45.8)
- added R906: TBD, Resistor_SMD:R_0805_2012Metric, F.Cu at (250.7, 48.7)
- added R907: TBD, Resistor_SMD:R_0805_2012Metric, F.Cu at (250.7, 51.6)
- added RN2001: 1k, Resistor_SMD:R_Array_Convex_4x0612, F.Cu at (107.2, 39.1)
- added RN2002: 1k, Resistor_SMD:R_Array_Convex_4x0612, F.Cu at (107.0, 48.1)
- added RN2003: 100R, Resistor_SMD:R_Array_Convex_4x0612, F.Cu at (107.0, 50.9)
- added RN2004: 100R, Resistor_SMD:R_Array_Convex_4x0612, F.Cu at (107.0, 55.7)
- added RN2101: 1k, Resistor_SMD:R_Array_Convex_4x0612, F.Cu at (129.6, 41.4)
- added RN2102: 1k, Resistor_SMD:R_Array_Convex_4x0612, F.Cu at (129.4, 50.4)
- added RN2103: 100R, Resistor_SMD:R_Array_Convex_4x0612, F.Cu at (129.4, 53.2)
- added RN2104: 100R, Resistor_SMD:R_Array_Convex_4x0612, F.Cu at (129.4, 58.0)
- added TP1001: TestPoint, TestPoint:TestPoint_Pad_D1.0mm, F.Cu at (153.3, 101.3)
- added TP2001: TestPoint, TestPoint:TestPoint_Pad_D1.0mm, F.Cu at (110.8, 39.3)
- added TP2002: TestPoint, TestPoint:TestPoint_Pad_D1.0mm, F.Cu at (109.8, 53.1)
- added TP2003: TestPoint, TestPoint:TestPoint_Pad_D1.0mm, F.Cu at (103.8, 51.7)
- added TP2004: TestPoint, TestPoint:TestPoint_Pad_D1.0mm, F.Cu at (110.2, 56.5)
- added TP2005: TestPoint, TestPoint:TestPoint_Pad_D1.0mm, F.Cu at (103.8, 56.5)
- added TP2101: TestPoint, TestPoint:TestPoint_Pad_D1.0mm, F.Cu at (133.2, 41.6)
- added TP2102: TestPoint, TestPoint:TestPoint_Pad_D1.0mm, F.Cu at (132.2, 55.4)
- added TP2103: TestPoint, TestPoint:TestPoint_Pad_D1.0mm, F.Cu at (126.2, 54.0)
- added TP2104: TestPoint, TestPoint:TestPoint_Pad_D1.0mm, F.Cu at (132.6, 58.8)
- added TP2105: TestPoint, TestPoint:TestPoint_Pad_D1.0mm, F.Cu at (126.2, 58.8)
- added TP803: TestPoint, TestPoint:TestPoint_Pad_D1.0mm, F.Cu at (148.2, 101.3)
- added TP903: TestPoint, TestPoint:TestPoint_Pad_D1.0mm, F.Cu at (278.1, 41.4)
- added TP904: TestPoint, TestPoint:TestPoint_Pad_D1.0mm, F.Cu at (278.1, 44.9)
- added U2001: OPA690xDBV, Package_TO_SOT_SMD:SOT-23-6, F.Cu at (108.9, 35.9)
- added U2002: AD8139, Package_SO:SOIC-8_5.3x5.3mm_P1.27mm, F.Cu at (107.2, 43.7)
- added U2101: OPA690xDBV, Package_TO_SOT_SMD:SOT-23-6, F.Cu at (131.3, 38.2)
- added U2102: AD8139, Package_SO:SOIC-8_5.3x5.3mm_P1.27mm, F.Cu at (129.6, 46.0)
- added U904: AP2112K-2.5, Package_TO_SOT_SMD:SOT-23-5, F.Cu at (261.1, 62.2)
- added U905: TPS62932, Package_TO_SOT_SMD:SOT-583-8, F.Cu at (272.5, 52.5)
- TP1101, TP1401, TP1402, TP1601, TP1602, TP1603, TP1604, TP1605, TP401, TP402, TP501, TP502, TP801, TP802, TP901, TP902: footprint TestPoint:TestPoint_Pad_D1.5mm -> TestPoint:TestPoint_Pad_D1.0mm
- moved C1301 163.5 mm to (287.5, 69.2)
- moved C1302 163.5 mm to (287.5, 72.2)
- moved C1303 163.5 mm to (287.5, 75.2)
- moved C1304 163.5 mm to (287.5, 78.2)
- moved U1301 163.5 mm to (292.3, 75.6)
- moved U1302 163.5 mm to (293.2, 70.0)
- moved C1601 161.0 mm to (94.2, 186.0)
- moved C1603 161.0 mm to (94.2, 192.0)
- moved C1604 161.0 mm to (94.2, 195.0)
- moved C1606 161.0 mm to (94.2, 201.0)
- moved C1607 161.0 mm to (94.2, 204.0)
- moved R1601 161.0 mm to (98.6, 185.9)
- moved R1603 161.0 mm to (98.6, 191.8)
- moved R1605 161.0 mm to (98.6, 197.7)
- moved R1606 161.0 mm to (98.6, 200.7)
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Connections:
- C1207 pad 1: /Digital Power/+3V3_D -> /ADC/+3V3_ADC
- C1208 pad 1: /Digital Power/+3V3_D -> /ADC/+3V3_ADC
- C1209 pad 1: /Digital Power/+3V3_D -> /ADC/+3V3_ADC
- C1210 pad 1: /Digital Power/+3V3_D -> /ADC/+3V3_ADC
- C1801 pad 1: /Digital Power/+3V3_D -> /ADC/+3V3_ADC
- C1802 pad 1: /Digital Power/+3V3_D -> /ADC/+3V3_ADC
- C1901 pad 1: /Digital Power/+3V3_D -> /ADC/+3V3_ADC
- C1902 pad 1: /Digital Power/+3V3_D -> /ADC/+3V3_ADC
- C1903 pad 1: /Digital Power/+3V3_D -> /ADC/+3V3_ADC
- C1904 pad 1: /Digital Power/+3V3_D -> /ADC/+3V3_ADC
- C701 pad 1: /Digital Power/+3V3_D -> /ADC/+3V3_ADC
- C702 pad 1: /Digital Power/+3V3_D -> /ADC/+3V3_ADC
- C703 pad 1: /Digital Power/+3V3_D -> /ADC/+3V3_ADC
- C704 pad 1: /Digital Power/+3V3_D -> /ADC/+3V3_ADC
- C901 pad 1: /Analog Power/+V_IN -> /Digital Power/3V7
- C902 pad 1: /Analog Power/+V_IN -> /Digital Power/3V7
- C904 pad 1: /Analog Power/+V_IN -> /Digital Power/3V7
- C905 pad 1: /Analog Power/+V_IN -> /Digital Power/3V7
- C907 pad 1: /Digital Power/+3V3_D -> /ADC/+3V3_ADC
- C909 pad 1: /Digital Power/+3V3_D -> /ADC/+3V3_ADC
- JP902 pad 1: /Analog Power/+V_IN -> /Digital Power/3V7
- JP903 pad 1: /Analog Power/+V_IN -> /Digital Power/3V7
- R1201 pad 2: /Digital Power/+3V3_D -> /ADC/+3V3_ADC
- R1203 pad 2: /Digital Power/+3V3_D -> /ADC/+3V3_ADC
- R1205 pad 2: /Digital Power/+3V3_D -> /ADC/+3V3_ADC
- R1206 pad 2: /Digital Power/+3V3_D -> /ADC/+3V3_ADC
- R1207 pad 2: /Digital Power/+3V3_D -> /ADC/+3V3_ADC
- R401 pad 2: /AFE/+2V5_AFE -> /SiPM Bias/+2V5_A
- R701 pad 1: /Digital Power/+3V3_D -> /ADC/+3V3_ADC
- R702 pad 1: /Digital Power/+3V3_D -> /ADC/+3V3_ADC
- TP901 pad 1: /Digital Power/+3V3_D -> /ADC/+3V3_ADC
- U1201 pad 8: /Digital Power/+3V3_D -> /ADC/+3V3_ADC
- U1801 pad 7: /Digital Power/+3V3_D -> /ADC/+3V3_ADC
- U601 pad 100: /Digital Power/+3V3_D -> /ADC/+3V3_ADC
- U601 pad 111: /Digital Power/+3V3_D -> /ADC/+3V3_ADC
- U601 pad 123: /Digital Power/+3V3_D -> /ADC/+3V3_ADC
- U601 pad 131: /Digital Power/+3V3_D -> /ADC/+3V3_ADC
- U601 pad 27: /Digital Power/+3V3_D -> /ADC/+3V3_ADC
- U601 pad 30: /Digital Power/+3V3_D -> /ADC/+3V3_ADC
- U601 pad 40: /Digital Power/+3V3_D -> /ADC/+3V3_ADC
- U601 pad 46: /Digital Power/+3V3_D -> /ADC/+3V3_ADC
- U601 pad 57: /Digital Power/+3V3_D -> /ADC/+3V3_ADC
- U601 pad 6: /Digital Power/+3V3_D -> /ADC/+3V3_ADC
- U601 pad 72: /Digital Power/+3V3_D -> /ADC/+3V3_ADC
- U601 pad 89: /Digital Power/+3V3_D -> /ADC/+3V3_ADC
- U601 pad 92: /Digital Power/+3V3_D -> /ADC/+3V3_ADC
- U902 pad 1: /Analog Power/+V_IN -> /Digital Power/3V7
- U902 pad 5: /Digital Power/+3V3_D -> /ADC/+3V3_ADC
- U903 pad 1: /Analog Power/+V_IN -> /Digital Power/3V7
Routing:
- net (no net): track 0.00 -> 176.3 mm
- net /ADC/+5V0_ADC: track 0.00 -> 151.5 mm, vias 0 -> 9
- net /AFE/-5V0_AFE: track 0.00 -> 139.5 mm, vias 0 -> 7
- net Net-(RN2001-R3.2): track 0.00 -> 49.6 mm
- net Net-(RN2001-R1.2): track 0.00 -> 35.7 mm
- net Net-(RN2003-R3.1): track 0.00 -> 22.4 mm
- net Net-(RN2003-R1.1): track 0.00 -> 22.4 mm
- net Net-(RN2101-R3.2): track 0.00 -> 13.2 mm
- net Net-(RN2101-R1.2): track 0.00 -> 12.4 mm
- net Net-(RN2002-R1.1): track 0.00 -> 11.6 mm
- net Net-(RN2002-R4.1): track 0.00 -> 11.6 mm
- net /AFE/AFEChannel1/AFE_OUT_P: track 0.00 -> 11.2 mm
- net /AFE/AFEChannel1/AFE_OUT_N: track 0.00 -> 11.2 mm
- net Net-(RN2103-R1.1): track 0.00 -> 5.60 mm
- net Net-(RN2103-R3.1): track 0.00 -> 5.60 mm
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- added copper zone on In1.Cu, net /ADC/+5V0_ADC
- added copper zone on In1.Cu, net /AFE/-5V0_AFE
- removed copper zone on B.Cu, net (none)
- removed copper zone on F.Cu, net (none)
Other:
- copper layers 2 -> 4

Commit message: emi
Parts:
- added J301: RFShield_TwoPieces, GammaSpectrometer:BUD_CU-470_Shield, F.Cu at (131.8, 51.8)
- moved C2117 15.5 mm to (139.6, 67.6)
- moved C2115 15.5 mm to (147.0, 67.4)
- moved TP2104 15.5 mm to (146.6, 65.4)
- moved C1006 15.5 mm to (158.8, 63.0)
- moved C2001 15.5 mm to (119.0, 43.1)
- moved C2003 15.5 mm to (122.6, 37.7)
- moved C2004 15.5 mm to (119.0, 40.9)
- moved C2005 15.5 mm to (126.9, 42.1)
- moved C2006 15.5 mm to (114.6, 49.6)
- moved C2007 15.5 mm to (127.6, 48.5)
- moved C2008 15.5 mm to (124.0, 55.1)
- moved C2009 15.5 mm to (118.0, 55.1)
- moved C2011 15.5 mm to (127.6, 50.7)
- moved C2012 15.5 mm to (121.0, 59.9)
- moved C2013 15.5 mm to (121.0, 64.7)
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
